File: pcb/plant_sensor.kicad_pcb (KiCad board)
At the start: 2 copper layers, 5 parts, among them Y1 Crystal

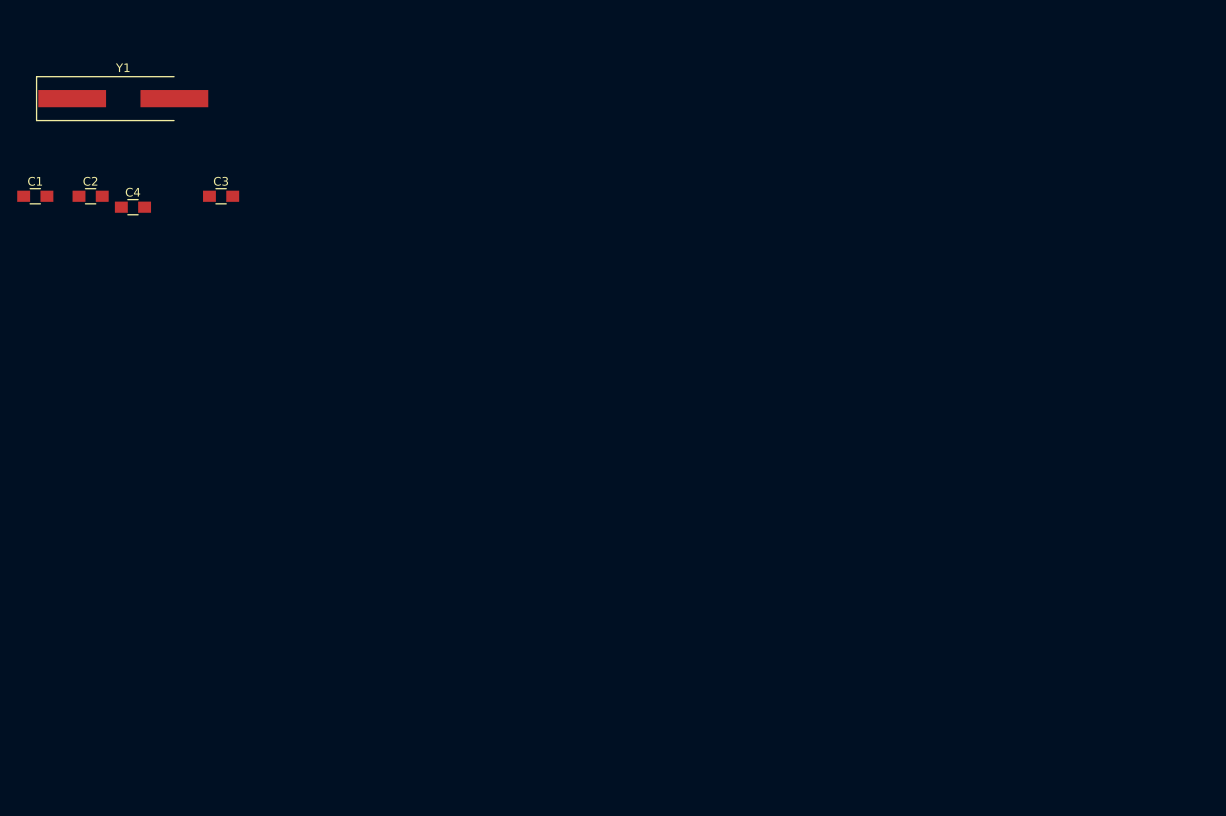
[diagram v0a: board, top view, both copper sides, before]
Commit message: Added UART and further work on schematics
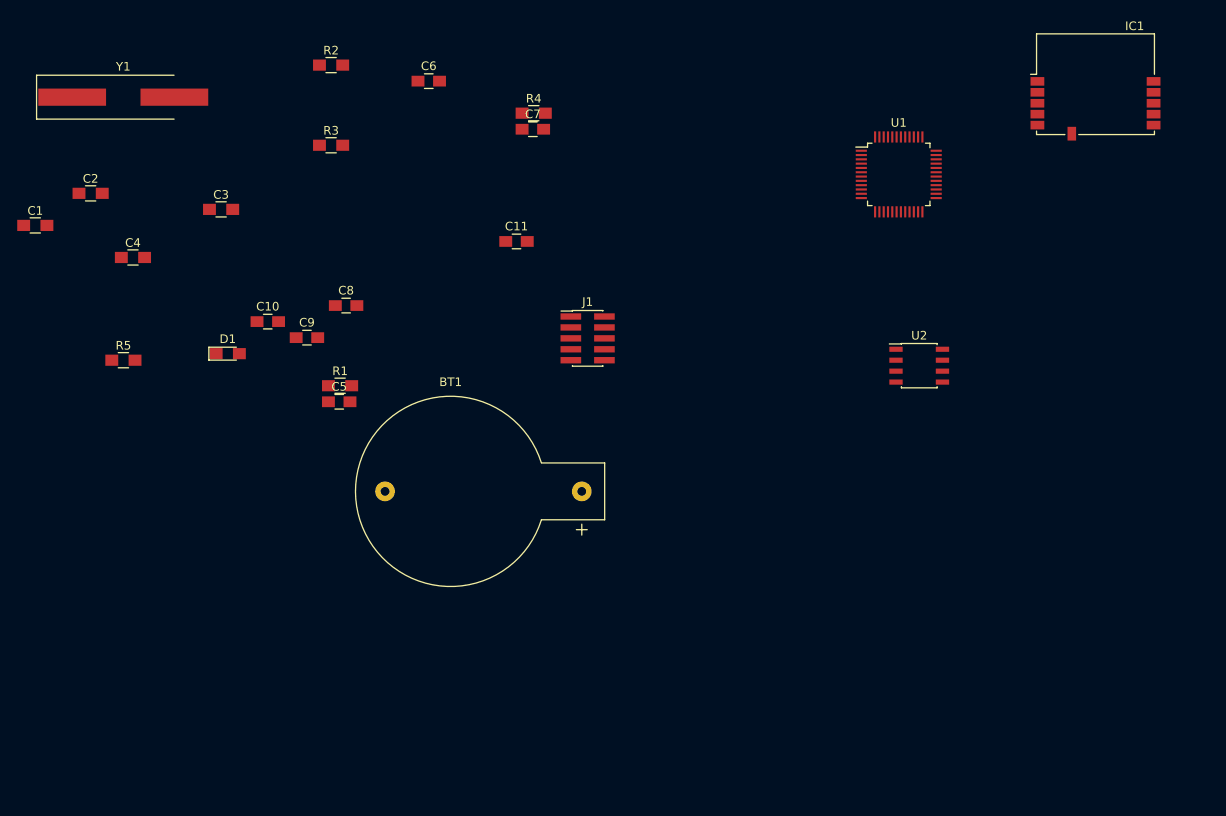
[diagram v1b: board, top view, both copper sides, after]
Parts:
- added BT1: CR2032, Connectors:CR2032H, F.Cu at (82.5, 68.6)
- added C10: 1uF X5R, Capacitors_SMD:C_0805_HandSoldering, F.Cu at (46.1, 48.9)
- added C11: 100nF, Capacitors_SMD:C_0805_HandSoldering, F.Cu at (75.0, 39.5)
- added C5: 1uF, Capacitors_SMD:C_0805_HandSoldering, F.Cu at (54.4, 58.2)
- added C6: 100nF, Capacitors_SMD:C_0805_HandSoldering, F.Cu at (64.8, 20.9)
- added C7: 100nF, Capacitors_SMD:C_0805_HandSoldering, F.Cu at (76.9, 26.5)
- added C8: 100nF, Capacitors_SMD:C_0805_HandSoldering, F.Cu at (55.2, 47.0)
- added C9: 100nF, Capacitors_SMD:C_0805_HandSoldering, F.Cu at (50.6, 50.7)
- added D1: RED, LEDs:LED_0805_HandSoldering, F.Cu at (41.4, 52.6)
- added IC1: SPBTLE-RF0, RF_Modules:ST_SPBTLE, F.Cu at (142.2, 24.1)
- added J1: Conn_ARM_JTAG_SWD_10, Pin_Headers:Pin_Header_Straight_2x05_Pitch1.27mm_SMD, F.Cu at (83.2, 50.8)
- added R1: 47K, Resistors_SMD:R_0805_HandSoldering, F.Cu at (54.5, 56.3)
- added R2: 10K, Resistors_SMD:R_0805_HandSoldering, F.Cu at (53.4, 19.1)
- added R3: 10K, Resistors_SMD:R_0805_HandSoldering, F.Cu at (53.4, 28.4)
- added R4: 1K, Resistors_SMD:R_0805_HandSoldering, F.Cu at (77.0, 24.6)
- added R5: FBead, Resistors_SMD:R_0805_HandSoldering, F.Cu at (29.3, 53.3)
- added U1: STM32L053C8Tx, Housings_QFP:LQFP-48_7x7mm_Pitch0.5mm, F.Cu at (119.4, 31.8)
- added U2: M95256-WMN6P, Housings_SOIC:SOIC-8_3.9x4.9mm_Pitch1.27mm, F.Cu at (121.8, 54.0)
- Y1: value Crystal -> 8MHz
- moved C4 5.84 mm to (30.4, 41.4)
- moved C1 3.39 mm to (19.1, 37.7)
- moved C3 1.52 mm to (40.6, 35.8)
- moved C2 0.34 mm to (25.5, 34.0)
- moved Y1 0.17 mm to (29.3, 22.8)
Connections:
- C2 pad 1: Net-(C2-Pad1) -> /RCC_OSC32_IN
- C4 pad 1: Net-(C4-Pad1) -> /RCC_OSC32_OUT

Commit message: Smaller MCU updated schematics
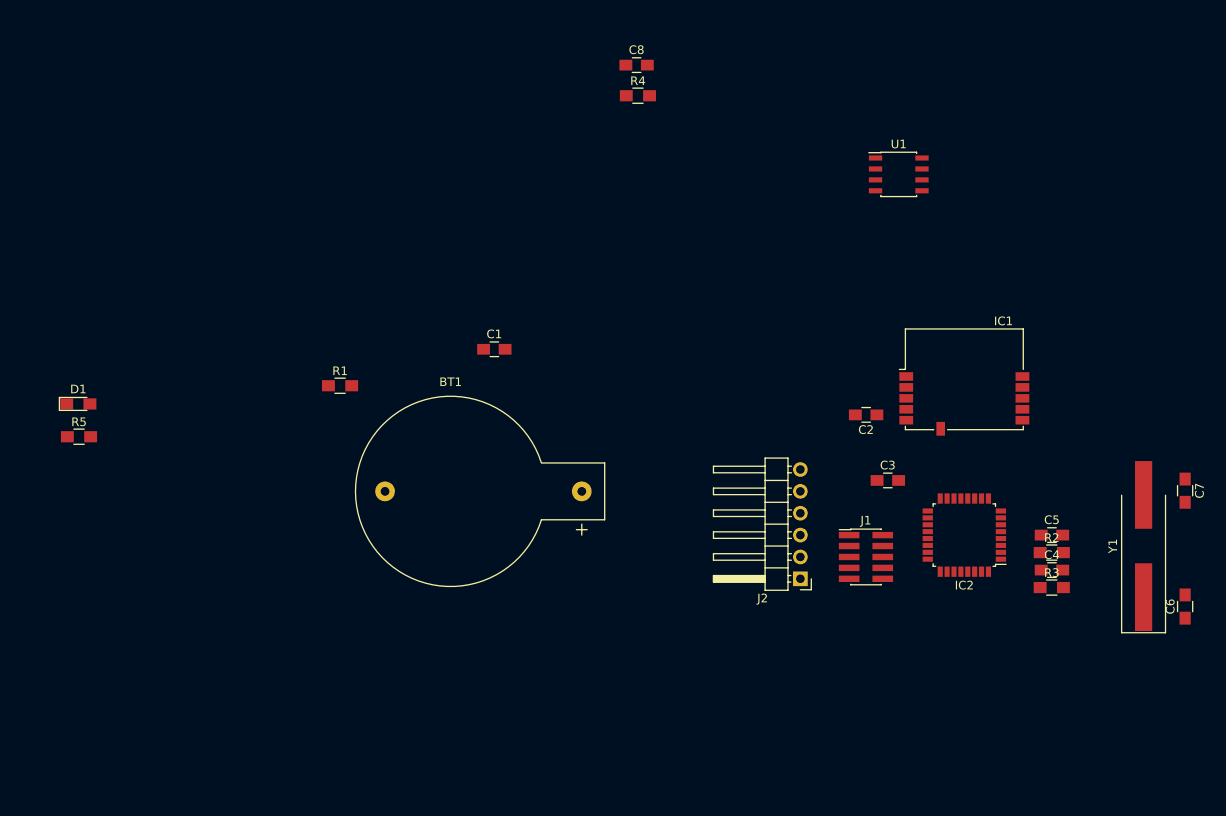
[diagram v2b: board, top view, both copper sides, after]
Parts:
- removed C10: 1uF X5R, Capacitors_SMD:C_0805_HandSoldering
- removed C11, C9: 100nF, Capacitors_SMD:C_0805_HandSoldering
- removed U2: M95256-WMN6P, Housings_SOIC:SOIC-8_3.9x4.9mm_Pitch1.27mm
- added IC2: STM32L052K8Tx, Housings_QFP:LQFP-32_7x7mm_Pitch0.8mm, F.Cu at (127.0, 73.7)
- added J2: COM, Pin_Headers:Pin_Header_Angled_1x06_Pitch2.54mm, F.Cu at (108.0, 78.7)
- C1: value 20pF -> 1uF X5R; footprint Resistors_SMD:R_0805_HandSoldering -> Capacitors_SMD:C_0805_HandSoldering
- C2: value 4.3pF -> 1uF; footprint Resistors_SMD:R_0805_HandSoldering -> Capacitors_SMD:C_0805_HandSoldering
- C3: value 20pF -> 100nF; footprint Resistors_SMD:R_0805_HandSoldering -> Capacitors_SMD:C_0805_HandSoldering
- C4: value 4.3pF -> 100nF; footprint Resistors_SMD:R_0805_HandSoldering -> Capacitors_SMD:C_0805_HandSoldering
- C5: value 1uF -> 100nF
- C6, C7: value 100nF -> 4.3pF; footprint Capacitors_SMD:C_0805_HandSoldering -> Resistors_SMD:R_0805_HandSoldering
- R2: value 10K -> FBead
- R4: value 1K -> 10K
- R5: value FBead -> 1K
- U1: value STM32L053C8Tx -> M95256-WMN6P; footprint Housings_QFP:LQFP-48_7x7mm_Pitch0.5mm -> Housings_SOIC:SOIC-8_3.9x4.9mm_Pitch1.27mm
- Y1: value 8MHz -> 32.768kHz
- moved Y1 129.5 mm to (147.8, 74.9), turned to 90 degrees
- moved C4 112.8 mm to (137.2, 77.7)
- moved C6 107.0 mm to (152.7, 82.0), turned to 90 degrees
- moved R2 101.1 mm to (137.2, 75.7)
- moved R3 98.3 mm to (137.2, 79.8)
- moved C2 93.7 mm to (115.6, 59.7), turned to 180 degrees
- moved C7 86.6 mm to (152.7, 68.5), turned to 270 degrees
- moved C5 84.3 mm to (137.2, 73.7)
- moved C3 83.6 mm to (118.1, 67.3)
- moved C1 55.2 mm to (72.4, 52.1)
- moved C8 43.8 mm to (88.9, 19.1)
- moved J1 41.1 mm to (115.6, 76.2)
- moved IC1 37.5 mm to (127.0, 58.4)
- moved D1 18.3 mm to (24.1, 58.4)
- moved R4 12.3 mm to (89.1, 22.6)
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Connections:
- net /BLE/SPI_BLE_nRESET renamed /BLE/BLE_nRESET
- C1 pad 1: /RCC_OSC_IN -> +BATT
- C2 pad 1: /RCC_OSC32_IN -> +3V3
- C3 pad 1: /RCC_OSC_OUT -> +3V3
- C4 pad 1: /RCC_OSC32_OUT -> +3V3
- C5 pad 1: +3V3 -> VDDA
- C6 pad 1: /nRESET -> /MCU/RCC_OSC32_IN
- C7 pad 1: +3V3 -> /MCU/RCC_OSC32_OUT
- C8 pad 1: +3V3 -> /MCU/nRESET
- IC1 pad 7: /BLE/SPI_CLK -> /MCU/SPI1_CLK
- IC1 pad 8: /BLE/SPI_MISO -> /MCU/SPI1_MISO
- IC1 pad 9: /BLE/SPI_MOSI -> /MCU/SPI1_MOSI
- J1 pad 10: /nRESET -> /MCU/nRESET
- J1 pad 2: /SYS_SWDIO -> /MCU/SYS_SWDIO
- J1 pad 4: /SYS_SWCLK -> /MCU/SYS_SWCLK
- R2 pad 2: /nRESET -> VDDA
- R3 pad 1: Net-(R3-Pad1) -> Net-(IC2-Pad31)
- R4 pad 1: Net-(R4-Pad1) -> +3V3
- R4 pad 2: Net-(D1-Pad2) -> /MCU/nRESET
- R5 pad 1: +3V3 -> Net-(R5-Pad1)
- R5 pad 2: VDDA -> Net-(D1-Pad2)
- U1 pad 1: +BATT -> Net-(U1-Pad1)
- U1 pad 3: /RCC_OSC32_IN -> Net-(U1-Pad3)
- U1 pad 4: /RCC_OSC32_OUT -> Net-(U1-Pad4)
- U1 pad 5: /RCC_OSC_IN -> Net-(U1-Pad5)
- U1 pad 6: /RCC_OSC_OUT -> Net-(U1-Pad6)
- U1 pad 7: /nRESET -> Net-(U1-Pad7)
- U1 pad 8: GND -> Net-(U1-Pad8)
- Y1 pad 1: /RCC_OSC_IN -> /MCU/RCC_OSC32_IN
- Y1 pad 2: /RCC_OSC_OUT -> /MCU/RCC_OSC32_OUT

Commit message: Added temperature sensor
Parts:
- added C9: 100nF, Capacitor_SMD:C_0805_2012Metric_Pad1.15x1.40mm_HandSolder, F.Cu at (98.8, 96.5)
- added U2: LM75B, Package_SO:SOIC-8_3.9x4.9mm_P1.27mm, F.Cu at (99.1, 101.6)
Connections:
- net Net-(R5-Pad1) renamed /MCU/LED
- IC2 pad 28: Net-(IC2-Pad28) -> /MCU/TEMP_IRQ
- IC2 pad 29: Net-(IC2-Pad29) -> /MCU/I2C1_SCL
- IC2 pad 30: Net-(IC2-Pad30) -> /MCU/I2C1_SDA
